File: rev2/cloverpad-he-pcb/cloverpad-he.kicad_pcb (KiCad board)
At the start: 2 copper layers, 70 x 75 mm, 51 parts, among them J1 USB_C_Receptacle_USB2.0, SW1 SW_Push, SW2 SW_Push, U1 SRV05-4, U2 XC6206P332MR, U3 DRV5056A4xDBZxQ1, U4 DRV5056A4xDBZxQ1, U5 DRV5056A4xDBZxQ1, U8 RP2040, U9 W25Q16JVSSIQ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

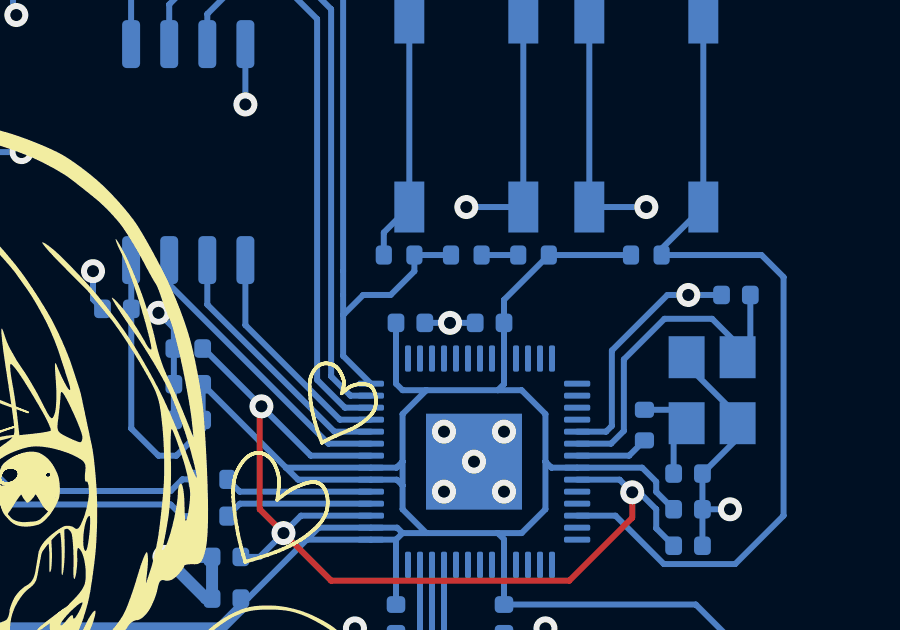
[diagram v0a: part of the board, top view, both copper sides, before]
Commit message: fix: use DRV5056A3 instead of A4
after some testing, losing the bottom 0.2mm of travel isn't a huge problem, and it's better to increase the resolution for the upper part of the keystroke instead.
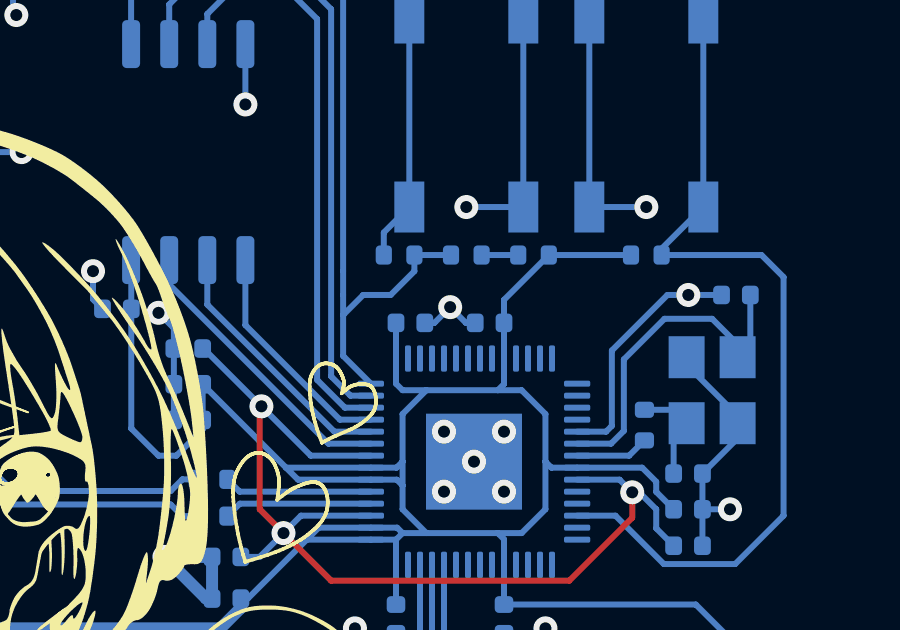
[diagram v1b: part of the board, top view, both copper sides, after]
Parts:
- U3, U4, U5: value DRV5056A4xDBZxQ1 -> DRV5056AxxDBZxQ1

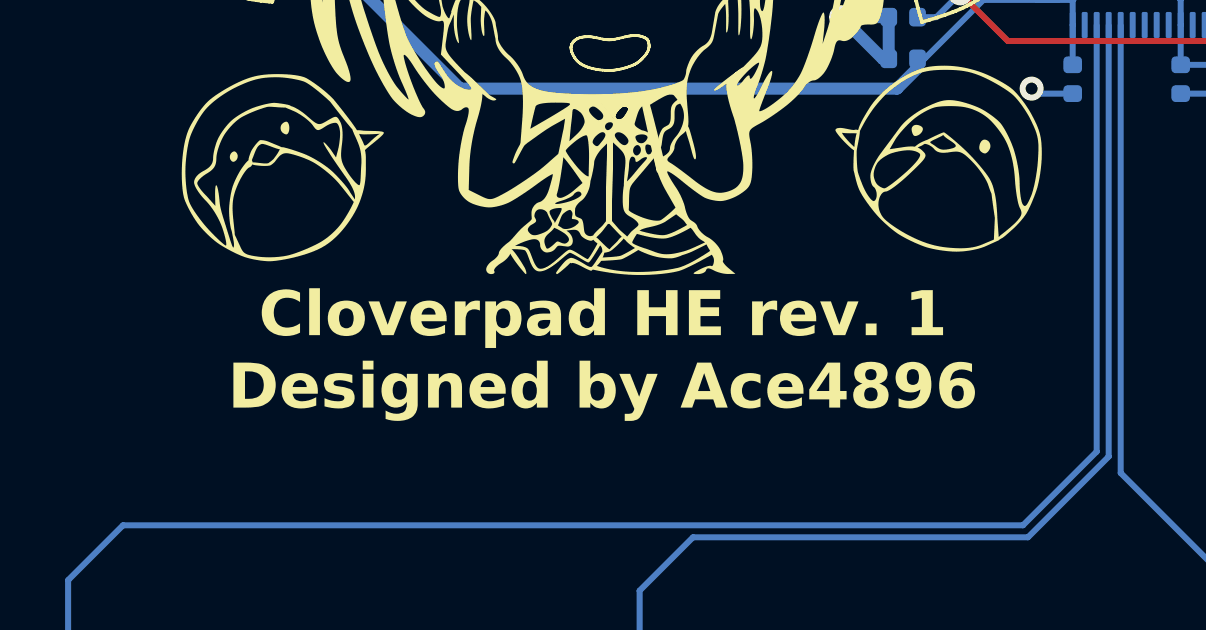
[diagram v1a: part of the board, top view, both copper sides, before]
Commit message: chore: update all symbols + footprints to match kicad 8
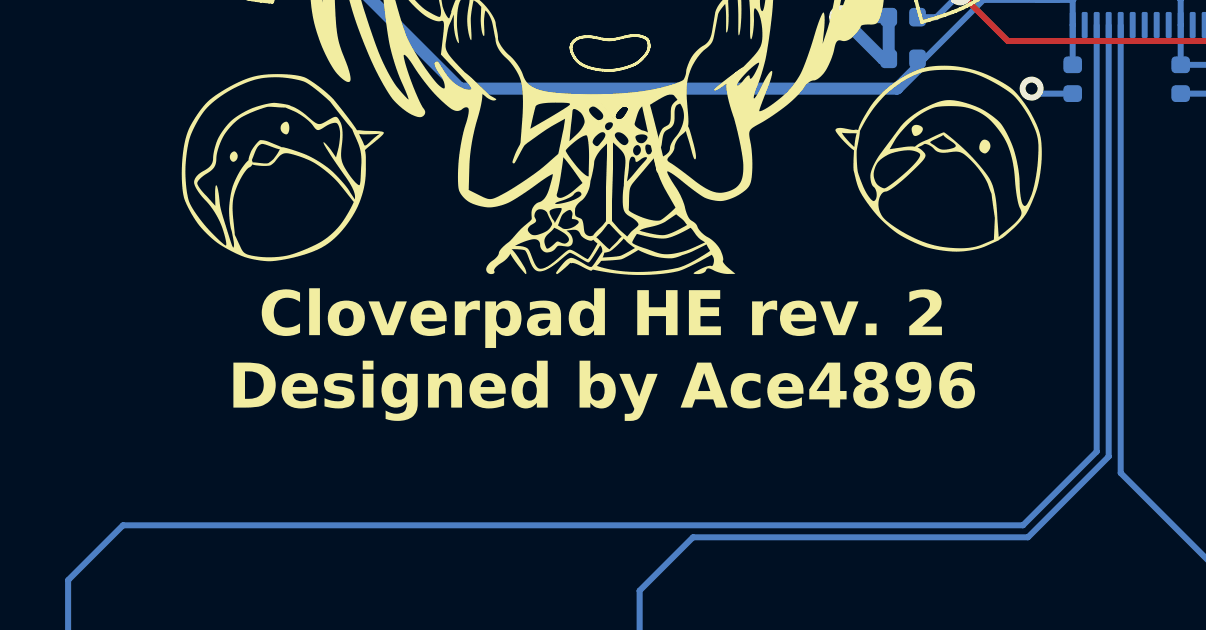
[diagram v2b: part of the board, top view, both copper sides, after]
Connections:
- J1 pad A8: unconnected-(J1-SBU1-PadA8) -> (no net)
- J1 pad B8: unconnected-(J1-SBU2-PadB8) -> (no net)
- U8 pad 24: SWCLK -> unconnected-(U8-SWCLK-Pad24)
- U8 pad 25: SWD -> unconnected-(U8-SWD-Pad25)
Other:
- board text added: "Cloverpad HE rev. 2 Designed by Ace4896"
- board text removed: "Cloverpad HE rev. 1 Designed by Ace4896"
